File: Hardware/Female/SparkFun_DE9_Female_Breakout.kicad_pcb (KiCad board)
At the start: 2 copper layers, 22.9 x 31.8 mm, 43 parts, among them J1 DE9 Female, J2 Conn_01x09, J3 Conn_01x01, J4 Conn_01x01

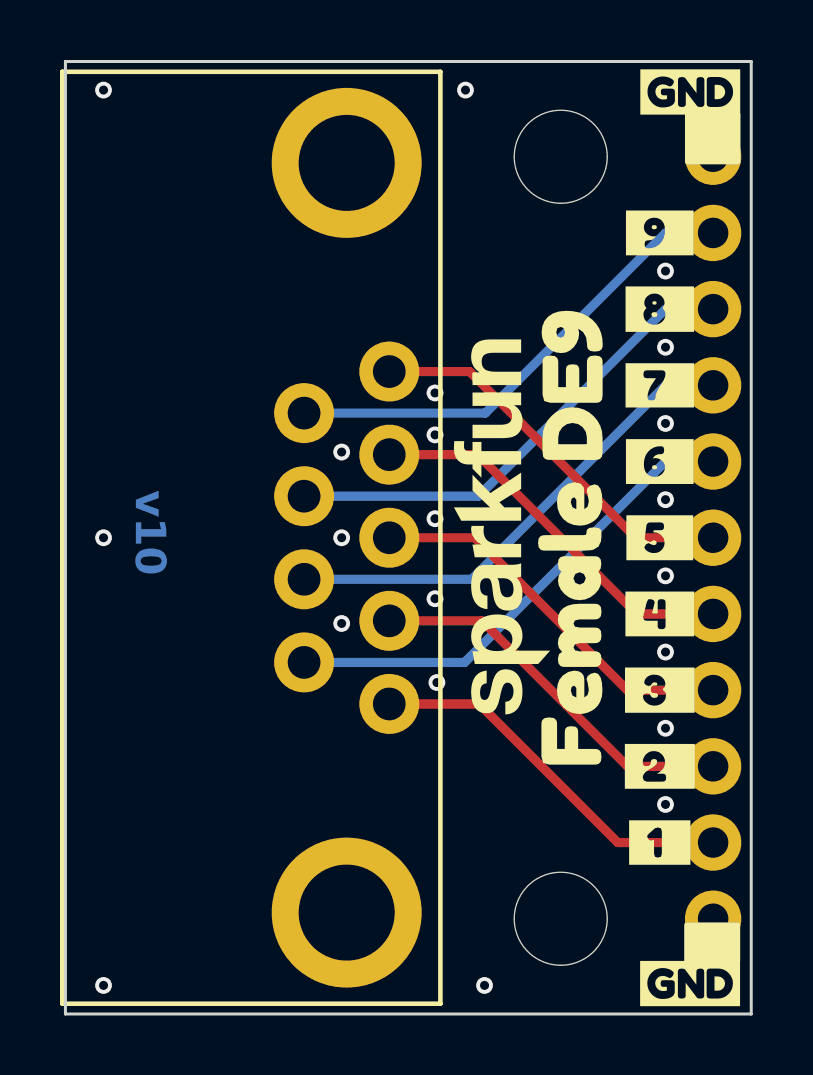
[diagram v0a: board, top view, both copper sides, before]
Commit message: Fix pin layout
Adds model for female socket
FIxes male footprint and symbol; updates schematic and PCB
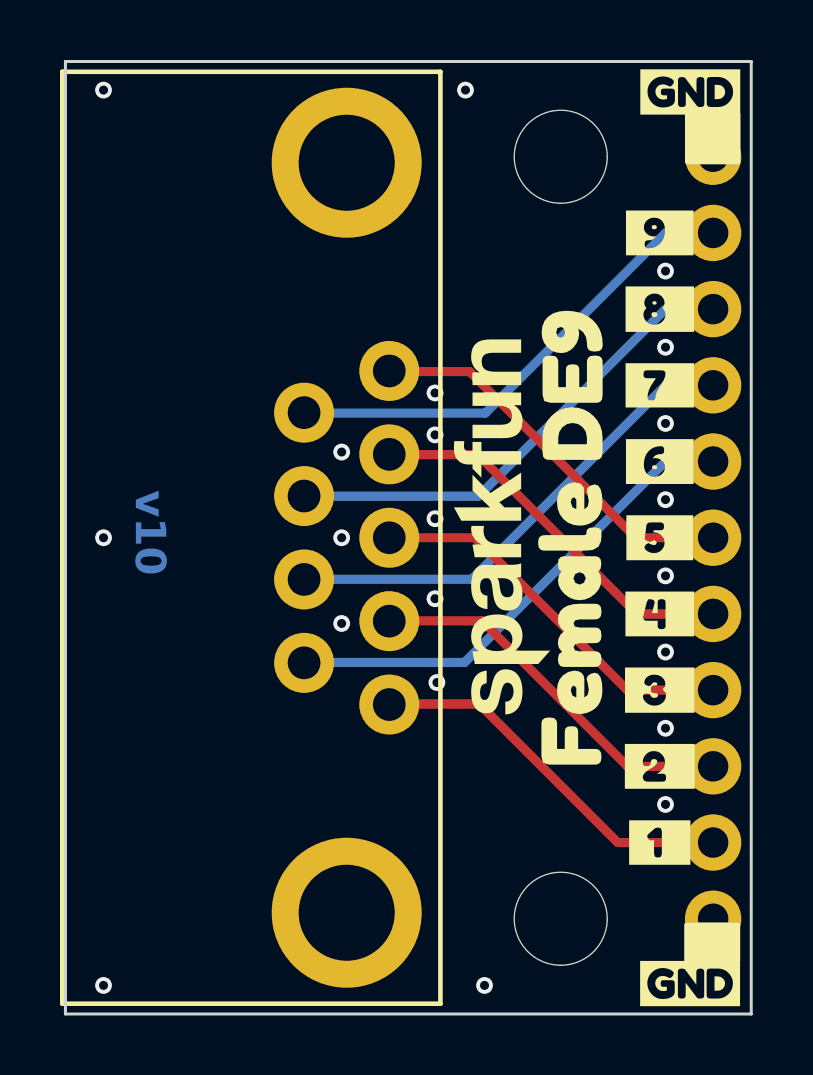
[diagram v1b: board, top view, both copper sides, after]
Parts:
- J1: footprint SparkFun-Connector:DE9_Female -> SparkFun-Connector:DE9_Socket_Horizontal_PTH
